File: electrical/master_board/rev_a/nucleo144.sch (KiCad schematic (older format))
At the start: 1 part, among them CN43 NUCLEO-F767ZI;2xF2x35

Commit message: Reworked Sonars, Servers, and LED's schematics.
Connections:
- no-connect marks 81 -> 120
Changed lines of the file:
@@
 $Descr A 11000 8500
 encoding utf-8
-Sheet 7 12
+Sheet 7 9
 Title "HR2 Master Board"
 Date "2020-10-03"
@@
 NoConn ~ 2450 6150
 NoConn ~ 2450 6250
-NoConn ~ 4900 1550
 NoConn ~ 5000 4800
 NoConn ~ 5000 4900
@@
 NoConn ~ 2000 950
 NoConn ~ 2000 1050
-NoConn ~ 4900 2750
-NoConn ~ 4900 2850
-NoConn ~ 4900 4050
-NoConn ~ 4900 4150
 NoConn ~ 7100 4550
 $Comp
@@
 Wire Wire Line
 	9750 3500 9750 3700
-Text HLabel 9950 2500 0    50   Input ~ 0
+Text HLabel 9850 2500 2    50   Input ~ 0
 LDR_TX
-Text HLabel 9950 2700 2    50   Output ~ 0
+Text HLabel 9850 2700 2    50   Output ~ 0
 LDR_SPIN
-Text HLabel 9950 2800 2    50   Output ~ 0
+Text HLabel 9850 2800 2    50   Output ~ 0
 LDR_EN
-Text HLabel 9950 2900 2    50   Output ~ 0
+Text HLabel 9850 2900 2    50   Output ~ 0
 LDR_PWM
-Text HLabel 9950 2600 2    50   Output ~ 0
+Text HLabel 9850 2600 2    50   Output ~ 0
 LDR_RX
-NoConn ~ 9950 2500
-NoConn ~ 9950 2600
-NoConn ~ 9950 2700
-NoConn ~ 9950 2800
-NoConn ~ 9950 2900
+NoConn ~ 9850 2500
+NoConn ~ 9850 2600
+NoConn ~ 9850 2700
+NoConn ~ 9850 2800
+NoConn ~ 9850 2900
 Text HLabel 8500 4800 2    50   Output ~ 0
 SERVO2
@@
 	8250 5000 8250 5800
 Connection ~ 8400 5000
+NoConn ~ 2200 2900
+NoConn ~ 2200 2800
+NoConn ~ 2450 4750
+NoConn ~ 5100 2950
+NoConn ~ 5100 3050
+NoConn ~ 5100 3150
+NoConn ~ 5100 3250
+NoConn ~ 5100 3350
+NoConn ~ 5100 3450
+NoConn ~ 5100 3550
+NoConn ~ 5100 3750
+NoConn ~ 5100 3850
+NoConn ~ 5100 3950
+NoConn ~ 5100 2750
+NoConn ~ 5100 2850
+NoConn ~ 5100 4050
+NoConn ~ 5100 4150
+NoConn ~ 5100 4250
+NoConn ~ 2450 5650
+NoConn ~ 5000 6100
+NoConn ~ 5000 6300
+NoConn ~ 2200 3800
+NoConn ~ 2200 3900
+NoConn ~ 2200 4000
+NoConn ~ 2200 4200
+NoConn ~ 2200 4300
+NoConn ~ 2200 3500
+NoConn ~ 2200 3600
+NoConn ~ 5000 5900
+NoConn ~ 5000 1250
+NoConn ~ 5000 1350
+NoConn ~ 5000 1550
+NoConn ~ 5000 1650
+NoConn ~ 5000 1950
+NoConn ~ 5000 2050
+NoConn ~ 5000 2150
+NoConn ~ 5000 2250
+NoConn ~ 5100 3650
+NoConn ~ 7900 2200
+NoConn ~ 7900 2500
+NoConn ~ 2450 5550
+NoConn ~ 5000 5300
+NoConn ~ 5000 5500
+NoConn ~ 5000 5800
+Text HLabel 9850 2050 2    50   Output ~ 0
+MISC_MOSI
+Text HLabel 9850 2150 2    50   Output ~ 0
+MISC_SCLK
+Text HLabel 9850 2250 2    50   Output ~ 0
+MISC_NSS
+Wire Wire Line
+	9750 2050 9850 2050
+Wire Wire Line
+	9850 2150 9750 2150
+Wire Wire Line
+	9850 2250 9750 2250
+Wire Wire Line
+	9750 2250 9750 2150
+Connection ~ 9750 2150
+Wire Wire Line
+	9750 2150 9750 2050
+Wire Wire Line
+	9750 2250 9750 3300
+Connection ~ 9750 2250
+Connection ~ 9750 3300
+Text HLabel 9850 1950 2    50   Output ~ 0
+DIO_NSS
+Wire Wire Line
+	9850 1950 9750 1950
+Wire Wire Line
+	9750 1950 9750 2050
+Connection ~ 9750 2050
 $EndSCHEMATC

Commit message: Lot's schematic work.
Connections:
- no-connect marks 120 -> 119
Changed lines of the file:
@@
 $Descr A 11000 8500
 encoding utf-8
-Sheet 7 9
+Sheet 8 9
 Title "HR2 Master Board"
 Date "2020-10-03"
@@
 Text HLabel 9850 3500 2    50   Output ~ 0
 LED_NSS
-Text HLabel 9850 3700 2    50   Output ~ 0
-TRIG1
-Text HLabel 9650 3700 0    50   Input ~ 0
+Text HLabel 9850 3700 2    50   Input ~ 0
 ECHO1
-Text HLabel 9850 3900 2    50   Output ~ 0
-TRIG2
-Text HLabel 9650 3900 0    50   Input ~ 0
+Text HLabel 9850 3800 2    50   Input ~ 0
 ECHO2
-Text HLabel 9850 4100 2    50   Output ~ 0
-TRIG3
-Text HLabel 9650 4100 0    50   Input ~ 0
+Text HLabel 9850 3900 2    50   Input ~ 0
 ECHO3
-Text HLabel 9850 4300 2    50   Output ~ 0
-TRIG4
-Text HLabel 9650 4300 0    50   Input ~ 0
+Text HLabel 9850 4000 2    50   Input ~ 0
 ECHO4
-Text HLabel 9850 4500 2    50   Output ~ 0
-TRIG5
-Text HLabel 9650 4500 0    50   Input ~ 0
+Text HLabel 9850 4100 2    50   Input ~ 0
 ECHO5
-Text HLabel 9850 4700 2    50   Output ~ 0
-TRIG6
-Text HLabel 9650 4700 0    50   Input ~ 0
+Text HLabel 9850 4200 2    50   Input ~ 0
 ECHO6
-Text HLabel 9850 4900 2    50   Output ~ 0
-TRIG7
-Text HLabel 9650 4900 0    50   Input ~ 0
+Text HLabel 9850 4300 2    50   Input ~ 0
 ECHO7
 Wire Wire Line
-	9650 3700 9750 3700
-Wire Wire Line
-	9850 3900 9650 3900
-Wire Wire Line
-	9650 4100 9850 4100
-Wire Wire Line
-	9650 4300 9850 4300
-Wire Wire Line
-	9650 4500 9850 4500
-Wire Wire Line
-	9650 4700 9850 4700
-Wire Wire Line
-	9650 4900 9850 4900
-Wire Wire Line
-	9750 3300 9850 3300
-Connection ~ 9750 3700
-Wire Wire Line
-	9750 3700 9850 3700
-Wire Wire Line
-	9850 3400 9750 3400
-Wire Wire Line
-	9750 3300 9750 3400
-Connection ~ 9750 3400
-Wire Wire Line
-	9750 3400 9750 3500
-Wire Wire Line
-	9850 3500 9750 3500
-Connection ~ 9750 3500
-Wire Wire Line
-	9750 3500 9750 3700
-Text HLabel 9850 2500 2    50   Input ~ 0
+	9850 3700 9650 3700
+Wire Wire Line
+	9650 3300 9850 3300
+Wire Wire Line
+	9850 3400 9650 3400
+Wire Wire Line
+	9650 3300 9650 3400
+Connection ~ 9650 3400
+Wire Wire Line
+	9650 3400 9650 3500
+Wire Wire Line
+	9850 3500 9650 3500
+Connection ~ 9650 3500
+Wire Wire Line
+	9650 3500 9650 3700
+Text HLabel 9850 2900 2    50   Input ~ 0
 LDR_TX
-Text HLabel 9850 2700 2    50   Output ~ 0
-LDR_SPIN
-Text HLabel 9850 2800 2    50   Output ~ 0
-LDR_EN
-Text HLabel 9850 2900 2    50   Output ~ 0
+Text HLabel 9850 3100 2    50   Output ~ 0
 LDR_PWM
-Text HLabel 9850 2600 2    50   Output ~ 0
+Text HLabel 9850 3000 2    50   Output ~ 0
 LDR_RX
-NoConn ~ 9850 2500
-NoConn ~ 9850 2600
-NoConn ~ 9850 2700
-NoConn ~ 9850 2800
-NoConn ~ 9850 2900
 Text HLabel 8500 4800 2    50   Output ~ 0
 SERVO2
@@
 NoConn ~ 2200 3600
 NoConn ~ 5000 5900
-NoConn ~ 5000 1250
-NoConn ~ 5000 1350
-NoConn ~ 5000 1550
-NoConn ~ 5000 1650
-NoConn ~ 5000 1950
-NoConn ~ 5000 2050
-NoConn ~ 5000 2150
-NoConn ~ 5000 2250
+NoConn ~ 5100 1250
+NoConn ~ 5100 1350
+NoConn ~ 5100 1550
+NoConn ~ 5100 1650
+NoConn ~ 5100 1950
+NoConn ~ 5100 2050
+NoConn ~ 5100 2150
+NoConn ~ 5100 2250
 NoConn ~ 5100 3650
 NoConn ~ 7900 2200
@@
 NoConn ~ 5000 5500
 NoConn ~ 5000 5800
-Text HLabel 9850 2050 2    50   Output ~ 0
+Text HLabel 9850 2500 2    50   Output ~ 0
 MISC_MOSI
-Text HLabel 9850 2150 2    50   Output ~ 0
-MISC_SCLK
-Text HLabel 9850 2250 2    50   Output ~ 0
+Text HLabel 9850 2600 2    50   Output ~ 0
+MISC_SCK
+Text HLabel 9850 2700 2    50   Output ~ 0
 MISC_NSS
 Wire Wire Line
-	9750 2050 9850 2050
-Wire Wire Line
-	9850 2150 9750 2150
-Wire Wire Line
-	9850 2250 9750 2250
-Wire Wire Line
-	9750 2250 9750 2150
-Connection ~ 9750 2150
-Wire Wire Line
-	9750 2150 9750 2050
-Wire Wire Line
-	9750 2250 9750 3300
-Connection ~ 9750 2250
-Connection ~ 9750 3300
-Text HLabel 9850 1950 2    50   Output ~ 0
+	9650 2500 9850 2500
+Wire Wire Line
+	9850 2600 9650 2600
+Wire Wire Line
+	9850 2700 9650 2700
+Wire Wire Line
+	9650 2700 9650 2600
+Connection ~ 9650 2600
+Wire Wire Line
+	9650 2600 9650 2500
+Wire Wire Line
+	9650 2700 9650 3000
+Connection ~ 9650 2700
+Connection ~ 9650 3300
+Text HLabel 9850 2400 2    50   Output ~ 0
 DIO_NSS
 Wire Wire Line
-	9850 1950 9750 1950
-Wire Wire Line
-	9750 1950 9750 2050
-Connection ~ 9750 2050
+	9850 2400 9650 2400
+Wire Wire Line
+	9650 2400 9650 2500
+Connection ~ 9650 2500
+Wire Wire Line
+	9650 3100 9850 3100
+Wire Wire Line
+	9850 3000 9650 3000
+Wire Wire Line
+	9650 3000 9650 3100
+NoConn ~ 9850 2900
+Connection ~ 9650 3000
+Connection ~ 9650 3100
+Wire Wire Line
+	9650 3100 9650 3300
+Text HLabel 9850 900  2    50   Input ~ 0
+A0
+Text HLabel 9850 1000 2    50   Input ~ 0
+A1
+Text HLabel 9850 1100 2    50   BiDi ~ 0
+A4_SDA
+Text HLabel 9850 1200 2    50   BiDi ~ 0
+A5_SCL
+Text HLabel 9850 1300 2    50   Output ~ 0
+D0_RX
+Text HLabel 9850 1400 2    50   Input ~ 0
+D1_TX
+Text HLabel 9850 1500 2    50   Output ~ 0
+D10_NSS
+Text HLabel 9850 1600 2    50   Output ~ 0
+D11_PWM_MOSI
+Text HLabel 9850 1700 2    50   Input ~ 0
+D12_MISO
+Text HLabel 9850 1800 2    50   Output ~ 0
+D13_SCK
+Text HLabel 9850 1900 2    50   Output ~ 0
+NRST
+Text HLabel 9850 2000 2    50   Input ~ 0
+INT0
+Text HLabel 9850 2100 2    50   Input ~ 0
+INT1
+NoConn ~ 9850 2100
+NoConn ~ 9850 900
+NoConn ~ 9850 1000
+Wire Wire Line
+	9650 1300 9850 1300
+Connection ~ 9650 2400
+Wire Wire Line
+	9850 1600 9650 1600
+Connection ~ 9650 1600
+Wire Wire Line
+	9650 1600 9650 1500
+Wire Wire Line
+	9850 1500 9650 1500
+Connection ~ 9650 1500
+Wire Wire Line
+	9650 1500 9650 1300
+Wire Wire Line
+	9850 1800 9650 1800
+Connection ~ 9650 1800
+Wire Wire Line
+	9650 1800 9650 1600
+Wire Wire Line
+	9850 1100 9750 1100
+Wire Wire Line
+	9750 1100 9750 1200
+Wire Wire Line
+	9750 1200 9850 1200
+Wire Wire Line
+	9650 1800 9650 2400
+Wire Wire Line
+	9850 2000 9750 2000
+Wire Wire Line
+	9750 2000 9750 1900
+Wire Wire Line
+	9750 1900 9850 1900
+Wire Wire Line
+	9850 1700 9750 1700
+Wire Wire Line
+	9750 1700 9750 1400
+Wire Wire Line
+	9750 1400 9850 1400
 $EndSCHEMATC

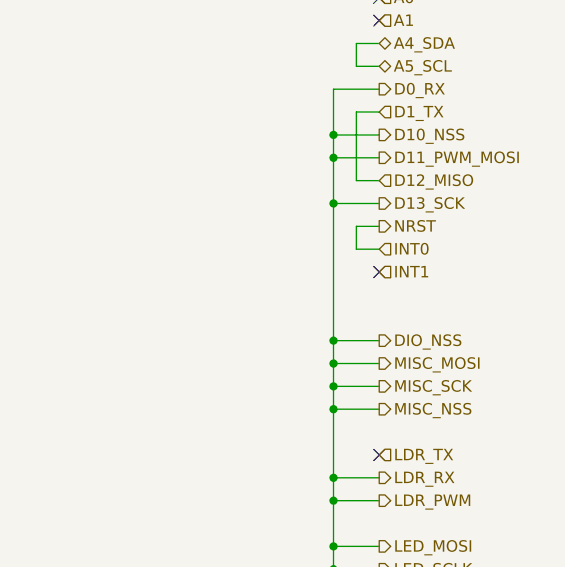
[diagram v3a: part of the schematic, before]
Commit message: Cleaned up schematics some.
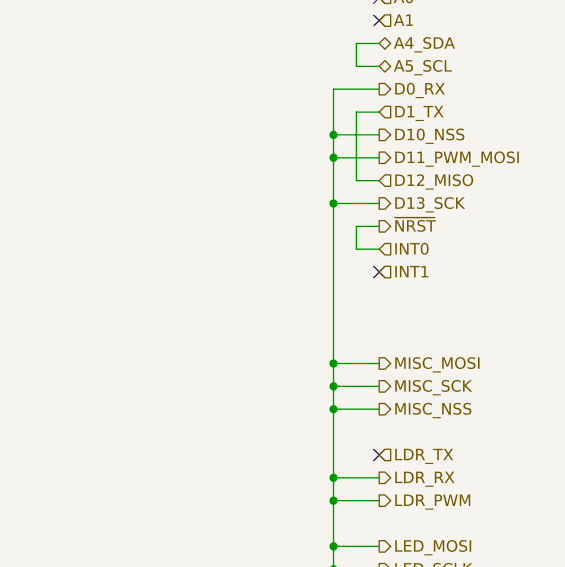
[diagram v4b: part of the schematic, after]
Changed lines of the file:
@@
 $Descr A 11000 8500
 encoding utf-8
-Sheet 8 9
+Sheet 9 9
 Title "HR2 Master Board"
 Date "2020-10-03"
@@
 Text HLabel 9850 3400 2    50   Output ~ 0
 LED_SCLK
-Text HLabel 9850 3500 2    50   Output ~ 0
-LED_NSS
 Text HLabel 9850 3700 2    50   Input ~ 0
 ECHO1
@@
 Text HLabel 9850 2900 2    50   Input ~ 0
 LDR_TX
-Text HLabel 9850 3100 2    50   Output ~ 0
-LDR_PWM
 Text HLabel 9850 3000 2    50   Output ~ 0
 LDR_RX
@@
 Connection ~ 9650 2700
 Connection ~ 9650 3300
-Text HLabel 9850 2400 2    50   Output ~ 0
-DIO_NSS
-Wire Wire Line
-	9850 2400 9650 2400
-Wire Wire Line
-	9650 2400 9650 2500
 Connection ~ 9650 2500
 Wire Wire Line
@@
 D13_SCK
 Text HLabel 9850 1900 2    50   Output ~ 0
-NRST
+~NRST
 Text HLabel 9850 2000 2    50   Input ~ 0
 INT0
@@
 Wire Wire Line
 	9650 1300 9850 1300
-Connection ~ 9650 2400
 Wire Wire Line
 	9850 1600 9650 1600
@@
 	9750 1200 9850 1200
 Wire Wire Line
-	9650 1800 9650 2400
-Wire Wire Line
 	9850 2000 9750 2000
 Wire Wire Line
@@
 Wire Wire Line
 	9750 1400 9850 1400
+Text HLabel 9850 3500 2    50   Output ~ 0
+LED_NSS
+Wire Wire Line
+	9650 1800 9650 2500
+Text HLabel 9850 3100 2    50   Output ~ 0
+LDR_PWM
 $EndSCHEMATC

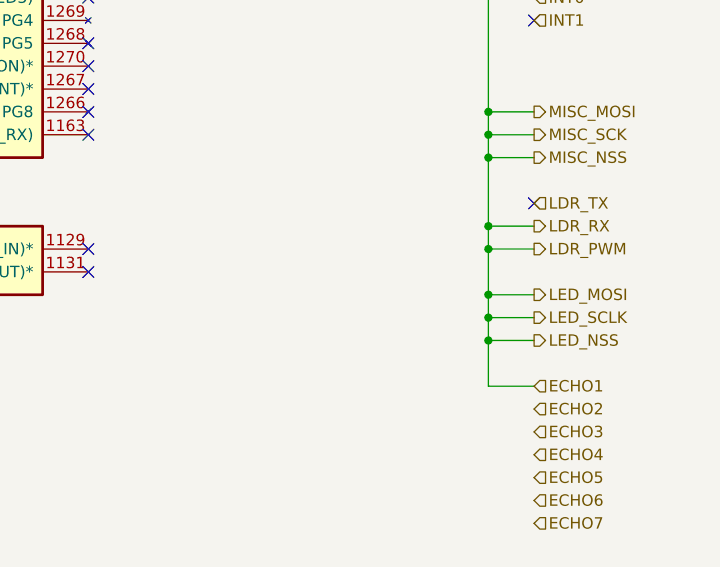
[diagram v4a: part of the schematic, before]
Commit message: Added WOWBus Schematic Sheet.
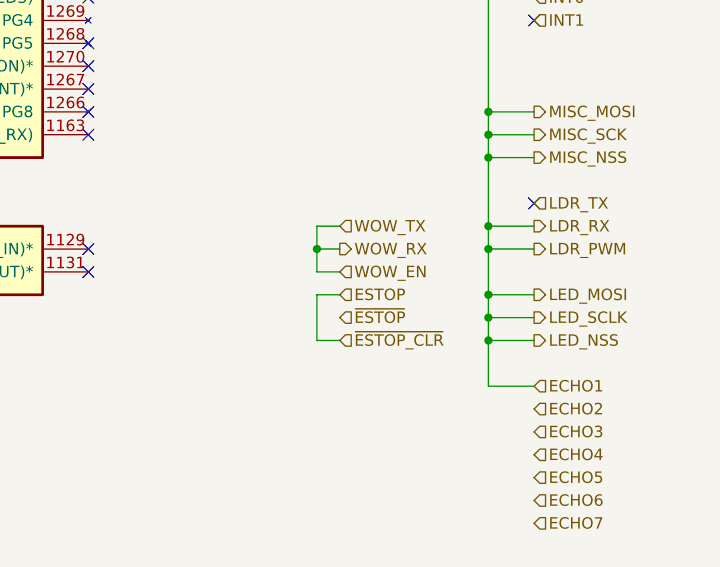
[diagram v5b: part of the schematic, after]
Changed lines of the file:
@@
 $Descr A 11000 8500
 encoding utf-8
-Sheet 9 9
+Sheet 9 10
 Title "HR2 Master Board"
-Date "2020-10-03"
+Date "2020-10-17"
 Rev "A"
 Comp "HomeBrew Robotics Club"
@@
 Text HLabel 9850 3100 2    50   Output ~ 0
 LDR_PWM
+Text HLabel 9000 3000 2    50   Input ~ 0
+WOW_TX
+Text HLabel 9000 3100 2    50   Output ~ 0
+WOW_RX
+Text HLabel 9000 3200 2    50   Input ~ 0
+WOW_EN
+Text HLabel 9000 3300 2    50   Input ~ 0
+ESTOP
+Text HLabel 9000 3400 2    50   Input ~ 0
+~ESTOP
+Text HLabel 9000 3500 2    50   Input ~ 0
+~ESTOP_CLR
+Wire Wire Line
+	9000 3000 8900 3000
+Wire Wire Line
+	8900 3000 8900 3100
+Wire Wire Line
+	8900 3200 9000 3200
+Wire Wire Line
+	9000 3100 8900 3100
+Connection ~ 8900 3100
+Wire Wire Line
+	8900 3100 8900 3200
+Wire Wire Line
+	9000 3300 8900 3300
+Wire Wire Line
+	8900 3300 8900 3500
+Wire Wire Line
+	8900 3500 9000 3500
 $EndSCHEMATC

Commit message: Wrapped up SBC sheet.
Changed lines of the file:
@@
 $Descr A 11000 8500
 encoding utf-8
-Sheet 9 10
+Sheet 8 10
 Title "HR2 Master Board"
 Date "2020-10-17"
@@
 Wire Wire Line
 	8900 3500 9000 3500
+Text HLabel 8500 4000 2    50   Output ~ 0
+SBC_TX
+Text HLabel 8500 4100 2    50   Input ~ 0
+SBC_RX
+Text HLabel 8500 4200 2    50   Input ~ 0
+SBC_ALIVE
+Text HLabel 8500 4300 2    50   Output ~ 0
+SBC_STOP
+Wire Wire Line
+	8500 4000 8400 4000
+Wire Wire Line
+	8400 4000 8400 4100
+Wire Wire Line
+	8400 4100 8500 4100
+Wire Wire Line
+	8500 4200 8400 4200
+Wire Wire Line
+	8400 4200 8400 4300
+Wire Wire Line
+	8400 4300 8500 4300
 $EndSCHEMATC

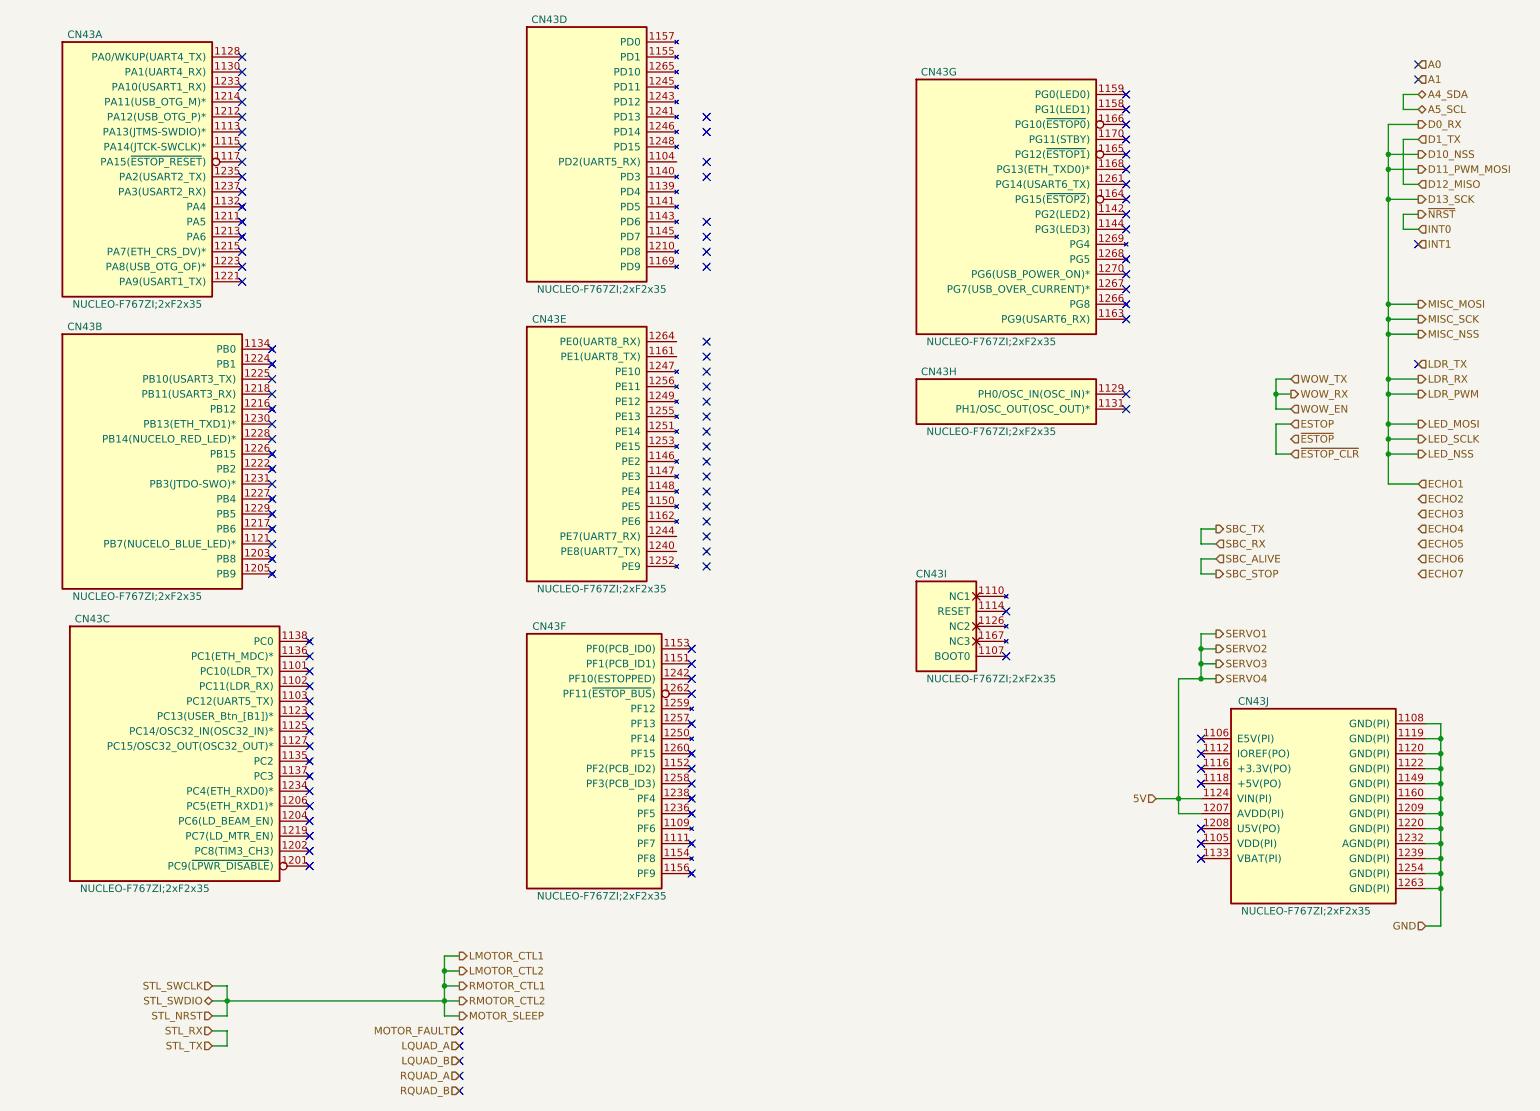
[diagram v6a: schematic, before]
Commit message: Bound signals to Morpho pins.
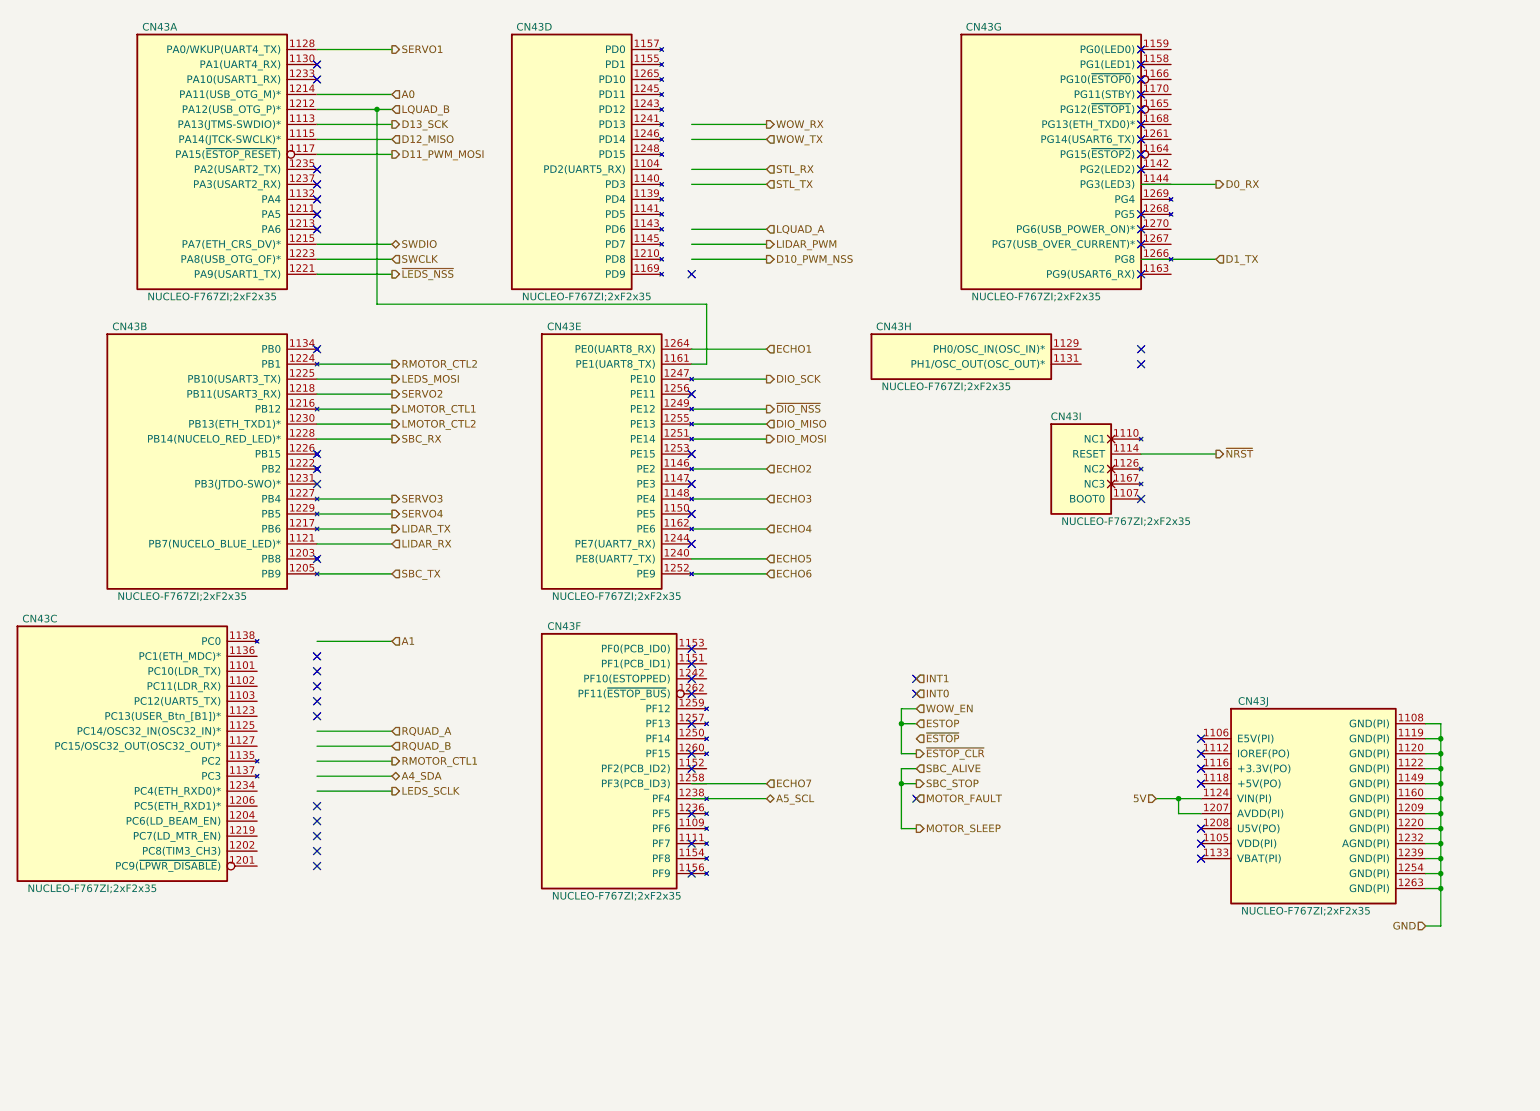
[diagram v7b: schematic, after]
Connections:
- net labels added: D10_PWM_NSS, DIO_MISO, DIO_MOSI, DIO_SCK, LEDS_MOSI, LEDS_SCLK, LIDAR_PWM, LIDAR_RX, LIDAR_TX, SWCLK, SWDIO, ~DIO_NSS, ~LEDS_NSS
- net labels removed: D10_NSS, LDR_PWM, LDR_RX, LDR_TX, LED_MOSI, LED_NSS, LED_SCLK, MISC_MOSI, MISC_NSS, MISC_SCK, STL_NRST, STL_SWCLK, STL_SWDIO
- wire segments 104 -> 92
- no-connect marks 119 -> 64
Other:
- moved on the sheet: CN43A, CN43B, CN43C, CN43D, CN43E, CN43F, CN43G, CN43H, CN43I

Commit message: Schematic is basically complete.
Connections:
- net labels added: ~ESTOP_IN, ~MOTOR_FAULT_IN, ~MOTOR_FAULT_OUT, ~MOTOR_SLEEP
- net labels removed: MOTOR_FAULT, MOTOR_SLEEP, SBC_STOP, ~ESTOP
- wire segments 92 -> 106
- no-connect marks 64 -> 58
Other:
- note added: "Cross Sheet Connetions"
- note added: "Morpho Power Pins."
- moved on the sheet: CN43A, CN43B, CN43C, CN43D, CN43E, CN43F, CN43G, CN43H, CN43I, CN43J
